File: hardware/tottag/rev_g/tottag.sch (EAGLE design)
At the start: 156 parts, among them J1 MICRO_USB_B_HIROSE_ZX62-B-5PA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, J2 CON_MICRO_SDDM3AT-SF-PEJM5, J3 TC2030-JLINK-NL, J4 TC2030-JLINK-NL, J5 TC2030-JLINK-NL, J7 TC2030-JLINK-NL, T1 HHM1595A1, U1 DW1000, U10 STM32F091CC, U11 AB1815-T3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

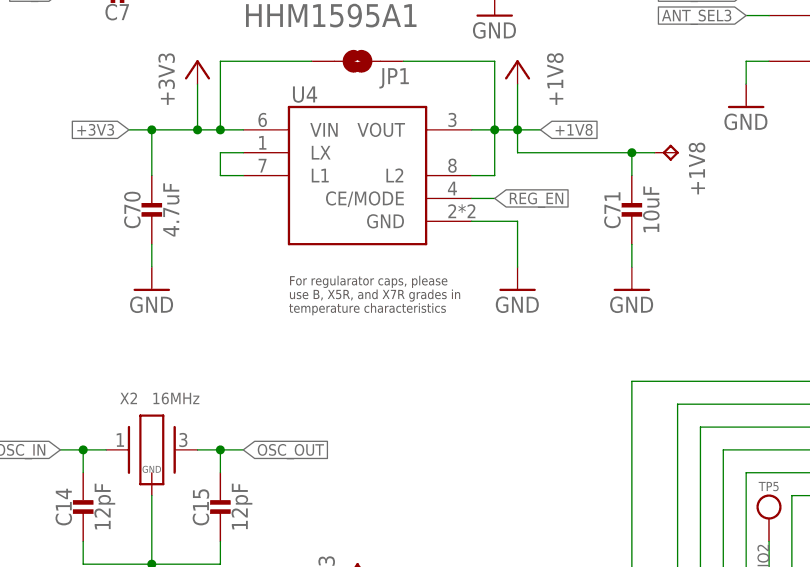
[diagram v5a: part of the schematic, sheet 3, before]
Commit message: rev_g: [WIP] Update planes; move BLE antenna
This location should keep the antenna from being covered by the primary battery
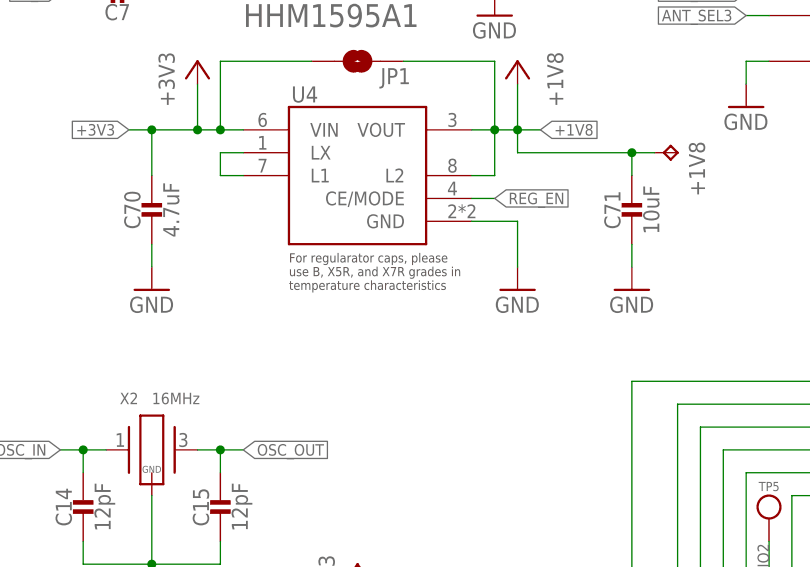
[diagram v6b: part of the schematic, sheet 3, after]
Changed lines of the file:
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@@
 for (DEEP)SLEEP</text>
 <text x="12.7" y="58.42" size="2.032" layer="98" rot="R180">VDD/48</text>
-<text x="38.1" y="137.16" size="1.016" layer="97">For regularator caps, please
+<text x="38.1" y="139.7" size="1.016" layer="97">For regularator caps, please
 use B, X5R, and X7R grades in
 temperature characteristics</text>

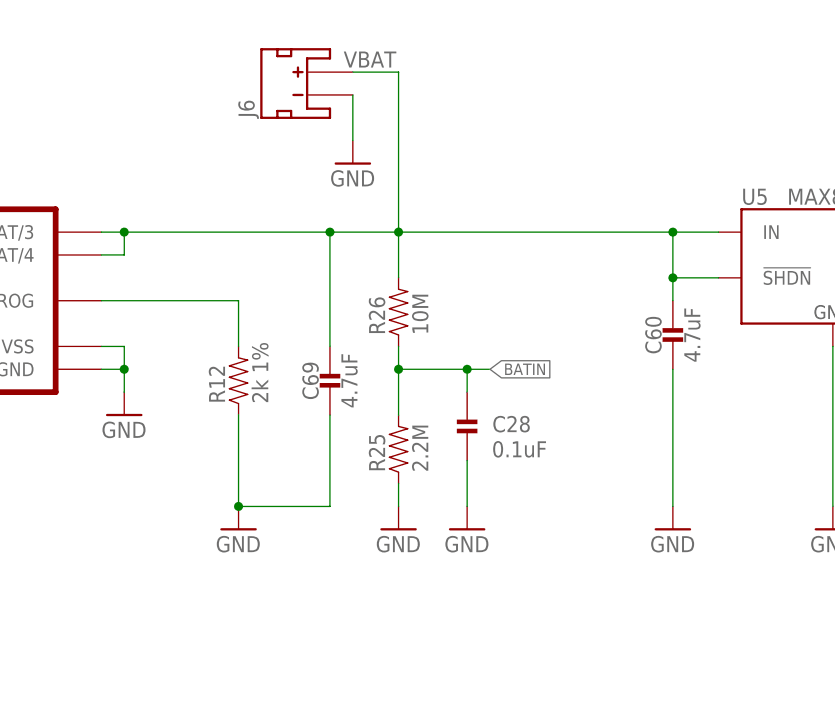
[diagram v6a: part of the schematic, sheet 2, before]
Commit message: rev_g: [WIP] add main power switch
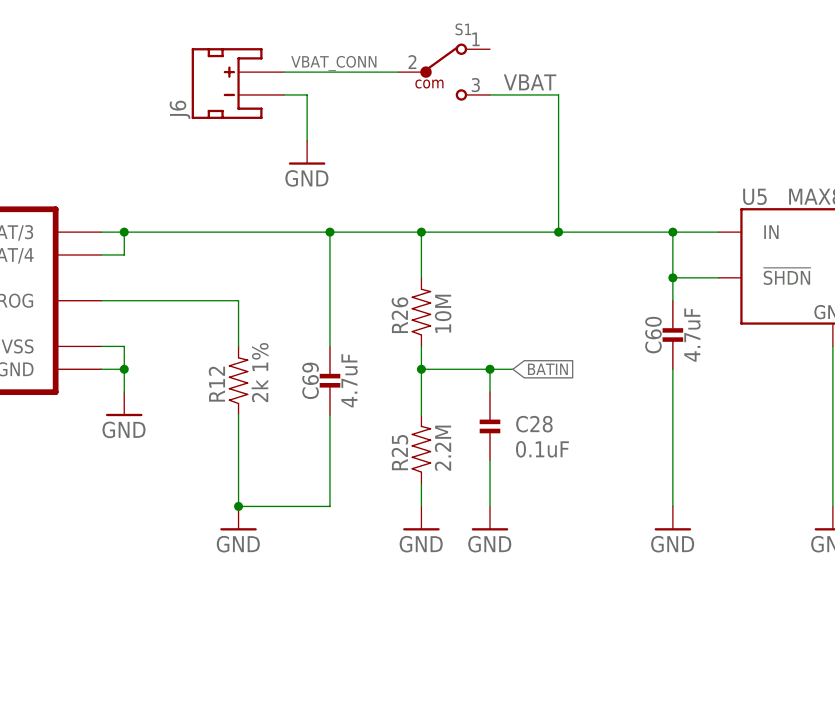
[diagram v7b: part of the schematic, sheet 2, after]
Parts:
- added S1: (no value), Wurth_Switch_WS-SLSU:450404015514
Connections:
- new net VBAT_CONN: J6.+, S1.2
- net VBAT: now also S1.3; no longer J6.+
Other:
- note added: "New case battery: PKCELL LP103450"
- note added: "To nRF ADC"
- moved on the sheet: C28, J6, R25, R26
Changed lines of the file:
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@@
 <part name="+3V5" library="regulators" deviceset="+3V3" device=""/>
 <part name="SUPPLY30" library="regulators" deviceset="GND" device=""/>
+<part name="S1" library="Wurth_Switch_WS-SLSU" library_urn="urn:adsk.eagle:library:18253886" deviceset="450404015514" device="" package3d_urn="urn:adsk.eagle:package:18253889/2"/>
 </parts>
 <sheets>
@@
 for optimal performance</text>
 <text x="222.758" y="140.97" size="1.778" layer="98" rot="R180" align="bottom-center">90 Ohm</text>
-<text x="112.522" y="179.07" size="1.778" layer="98" align="center-right">"Standard" battery is
+<text x="104.902" y="184.15" size="1.778" layer="98" align="center-right">"Standard" battery is
 PKCELL LP803860
 1528-1857-ND</text>
+<text x="104.902" y="173.99" size="1.778" layer="98" align="center-right">New case battery:
+PKCELL LP103450
+</text>
+<text x="146.304" y="149.098" size="1.27" layer="98">To nRF ADC</text>
 </plain>
 <instances>
@@
 <attribute name="VALUE" x="203.2" y="165.1" size="1.778" layer="96" rot="R90"/>
 </instance>
-<instance part="R26" gate="G$1" x="132.08" y="154.94" smashed="yes" rot="R90">
-<attribute name="NAME" x="130.5814" y="151.13" size="1.778" layer="95" rot="R90"/>
-<attribute name="VALUE" x="135.382" y="151.13" size="1.778" layer="96" rot="R90"/>
-</instance>
-<instance part="R25" gate="G$1" x="132.08" y="139.7" smashed="yes" rot="R90">
-<attribute name="NAME" x="130.5814" y="135.89" size="1.778" layer="95" rot="R90"/>
-<attribute name="VALUE" x="135.382" y="135.89" size="1.778" layer="96" rot="R90"/>
+<instance part="R26" gate="G$1" x="134.62" y="154.94" smashed="yes" rot="R90">
+<attribute name="NAME" x="133.1214" y="151.13" size="1.778" layer="95" rot="R90"/>
+<attribute name="VALUE" x="137.922" y="151.13" size="1.778" layer="96" rot="R90"/>
+</instance>
+<instance part="R25" gate="G$1" x="134.62" y="139.7" smashed="yes" rot="R90">
+<attribute name="NAME" x="133.1214" y="135.89" size="1.778" layer="95" rot="R90"/>
+<attribute name="VALUE" x="137.922" y="135.89" size="1.778" layer="96" rot="R90"/>
 </instance>
 <instance part="C60" gate="G$1" x="162.56" y="152.4" smashed="yes">
@@
 <attribute name="VALUE" x="207.01" y="151.13" size="1.778" layer="96" ratio="12" rot="R270" align="bottom-center"/>
 </instance>
-<instance part="C28" gate="G$1" x="139.7" y="139.7" smashed="yes" rot="R180">
-<attribute name="NAME" x="146.812" y="142.113" size="1.778" layer="95" rot="R180"/>
-<attribute name="VALUE" x="148.59" y="139.319" size="1.778" layer="96" rot="R180"/>
+<instance part="C28" gate="G$1" x="142.24" y="139.7" smashed="yes" rot="R180">
+<attribute name="NAME" x="149.352" y="142.113" size="1.778" layer="95" rot="R180"/>
+<attribute name="VALUE" x="151.13" y="139.319" size="1.778" layer="96" rot="R180"/>
 </instance>
 <instance part="SUPPLY3" gate="1" x="27.94" y="129.54" smashed="yes">
 <attribute name="VALUE" x="25.4" y="127" size="1.778" layer="96"/>
 </instance>
-<instance part="SUPPLY4" gate="1" x="132.08" y="129.54" smashed="yes">
-<attribute name="VALUE" x="129.54" y="127" size="1.778" layer="96"/>
-</instance>
-<instance part="SUPPLY7" gate="1" x="139.7" y="129.54" smashed="yes">
-<attribute name="VALUE" x="137.16" y="127" size="1.778" layer="96"/>
+<instance part="SUPPLY4" gate="1" x="134.62" y="129.54" smashed="yes">
+<attribute name="VALUE" x="132.08" y="127" size="1.778" layer="96"/>
+</instance>
+<instance part="SUPPLY7" gate="1" x="142.24" y="129.54" smashed="yes">
+<attribute name="VALUE" x="139.7" y="127" size="1.778" layer="96"/>
 </instance>
 <instance part="D1" gate="G$1" x="48.26" y="152.4" smashed="yes">
@@
 <attribute name="VALUE" x="12.7" y="144.78" size="1.778" layer="95" rot="MR0"/>
 </instance>
-<instance part="SUPPLY8" gate="1" x="127" y="170.18" smashed="yes">
-<attribute name="VALUE" x="124.46" y="167.64" size="1.778" layer="96"/>
+<instance part="SUPPLY8" gate="1" x="121.92" y="170.18" smashed="yes">
+<attribute name="VALUE" x="119.38" y="167.64" size="1.778" layer="96"/>
 </instance>
 <instance part="U5" gate="G$1" x="180.34" y="160.02" smashed="yes">
@@
 <attribute name="VALUE" x="230.378" y="158.75" size="1.778" layer="96" rot="R270"/>
 </instance>
-<instance part="J6" gate="G$1" x="121.92" y="177.8" smashed="yes" rot="R90">
-<attribute name="NAME" x="116.078" y="175.26" size="1.778" layer="95" rot="R90"/>
+<instance part="J6" gate="G$1" x="114.3" y="177.8" smashed="yes" rot="R90">
+<attribute name="NAME" x="108.458" y="175.26" size="1.778" layer="95" rot="R90"/>
+</instance>
+<instance part="S1" gate="G$1" x="137.16" y="180.34" smashed="yes">
+<attribute name="VALUE" x="134.75" y="175.22" size="1.27" layer="96"/>
+<attribute name="NAME" x="139.3" y="184.45" size="1.27" layer="95" align="bottom-center"/>
 </instance>
 </instances>
@@
 <pinref part="R25" gate="G$1" pin="1"/>
 <pinref part="SUPPLY4" gate="1" pin="GND"/>
-<wire x1="132.08" y1="134.62" x2="132.08" y2="132.08" width="0.1524" layer="91"/>
+<wire x1="134.62" y1="134.62" x2="134.62" y2="132.08" width="0.1524" layer="91"/>
 </segment>
 <segment>
 <pinref part="C28" gate="G$1" pin="1"/>
 <pinref part="SUPPLY7" gate="1" pin="GND"/>
-<wire x1="139.7" y1="137.16" x2="139.7" y2="132.08" width="0.1524" layer="91"/>
+<wire x1="142.24" y1="137.16" x2="142.24" y2="132.08" width="0.1524" layer="91"/>
 </segment>
 <segment>
@@
 <segment>
 <pinref part="SUPPLY8" gate="1" pin="GND"/>
-<wire x1="127" y1="172.72" x2="127" y2="177.8" width="0.1524" layer="91"/>
+<wire x1="121.92" y1="172.72" x2="121.92" y2="177.8" width="0.1524" layer="91"/>
+<wire x1="121.92" y1="177.8" x2="119.38" y2="177.8" width="0.1524" layer="91"/>
 <pinref part="J6" gate="G$1" pin="-"/>
 </segment>
@@
 <pinref part="R26" gate="G$1" pin="2"/>
 <wire x1="101.6" y1="162.56" x2="124.46" y2="162.56" width="0.1524" layer="91"/>
-<wire x1="124.46" y1="162.56" x2="132.08" y2="162.56" width="0.1524" layer="91"/>
-<wire x1="132.08" y1="162.56" x2="132.08" y2="157.48" width="0.1524" layer="91"/>
+<wire x1="124.46" y1="162.56" x2="134.62" y2="162.56" width="0.1524" layer="91"/>
+<wire x1="134.62" y1="162.56" x2="134.62" y2="157.48" width="0.1524" layer="91"/>
 <pinref part="C60" gate="G$1" pin="1"/>
 <wire x1="162.56" y1="154.94" x2="162.56" y2="157.48" width="0.1524" layer="91"/>
 <wire x1="162.56" y1="157.48" x2="162.56" y2="162.56" width="0.1524" layer="91"/>
-<wire x1="132.08" y1="162.56" x2="162.56" y2="162.56" width="0.1524" layer="91"/>
-<junction x="132.08" y="162.56"/>
+<wire x1="134.62" y1="162.56" x2="149.86" y2="162.56" width="0.1524" layer="91"/>
+<junction x="134.62" y="162.56"/>
 <junction x="162.56" y="162.56"/>
-<wire x1="132.08" y1="180.34" x2="132.08" y2="162.56" width="0.1524" layer="91"/>
-<wire x1="132.08" y1="180.34" x2="127" y2="180.34" width="0.1524" layer="91"/>
 <pinref part="U5" gate="G$1" pin="IN"/>
+<wire x1="149.86" y1="162.56" x2="162.56" y2="162.56" width="0.1524" layer="91"/>
 <wire x1="162.56" y1="162.56" x2="167.64" y2="162.56" width="0.1524" layer="91"/>
 <pinref part="U5" gate="G$1" pin="!SHDN"/>
@@
 <wire x1="101.6" y1="160.02" x2="101.6" y2="162.56" width="0.1524" layer="91"/>
 <junction x="101.6" y="162.56"/>
-<label x="131.826" y="180.848" size="1.778" layer="95" rot="MR0"/>
+<label x="149.606" y="178.308" size="1.778" layer="95" rot="MR0"/>
 <pinref part="C69" gate="G$1" pin="1"/>
 <wire x1="124.46" y1="162.56" x2="124.46" y2="149.86" width="0.1524" layer="91"/>
 <junction x="124.46" y="162.56"/>
-<pinref part="J6" gate="G$1" pin="+"/>
+<pinref part="S1" gate="G$1" pin="3"/>
+<wire x1="142.24" y1="177.8" x2="149.86" y2="177.8" width="0.1524" layer="91"/>
+<wire x1="149.86" y1="177.8" x2="149.86" y2="162.56" width="0.1524" layer="91"/>
+<junction x="149.86" y="162.56"/>
 </segment>
 </net>
 <net name="BATIN" class="0">
 <segment>
-<label x="142.24" y="147.32" size="1.27" layer="95" xref="yes"/>
+<label x="144.78" y="147.32" size="1.27" layer="95" xref="yes"/>
 <pinref part="C28" gate="G$1" pin="2"/>
 <pinref part="R26" gate="G$1" pin="1"/>
 <pinref part="R25" gate="G$1" pin="2"/>
-<wire x1="132.08" y1="142.24" x2="132.08" y2="147.32" width="0.1524" layer="91"/>
-<wire x1="132.08" y1="147.32" x2="132.08" y2="149.86" width="0.1524" layer="91"/>
-<wire x1="132.08" y1="147.32" x2="139.7" y2="147.32" width="0.1524" layer="91"/>
-<wire x1="139.7" y1="147.32" x2="139.7" y2="144.78" width="0.1524" layer="91"/>
-<junction x="132.08" y="147.32"/>
-<wire x1="139.7" y1="147.32" x2="142.24" y2="147.32" width="0.1524" layer="91"/>
-<junction x="139.7" y="147.32"/>
+<wire x1="134.62" y1="142.24" x2="134.62" y2="147.32" width="0.1524" layer="91"/>
+<wire x1="134.62" y1="147.32" x2="134.62" y2="149.86" width="0.1524" layer="91"/>
+<wire x1="134.62" y1="147.32" x2="142.24" y2="147.32" width="0.1524" layer="91"/>
+<wire x1="142.24" y1="147.32" x2="142.24" y2="144.78" width="0.1524" layer="91"/>
+<junction x="134.62" y="147.32"/>
+<wire x1="142.24" y1="147.32" x2="144.78" y2="147.32" width="0.1524" layer="91"/>
+<junction x="142.24" y="147.32"/>
 </segment>
 </net>
@@
 </segment>
 </net>
+<net name="VBAT_CONN" class="0">
+<segment>
+<pinref part="J6" gate="G$1" pin="+"/>
+<pinref part="S1" gate="G$1" pin="2"/>
+<wire x1="119.38" y1="180.34" x2="132.08" y2="180.34" width="0.1524" layer="91"/>
+<label x="120.142" y="180.848" size="1.27" layer="95"/>
+</segment>
+</net>

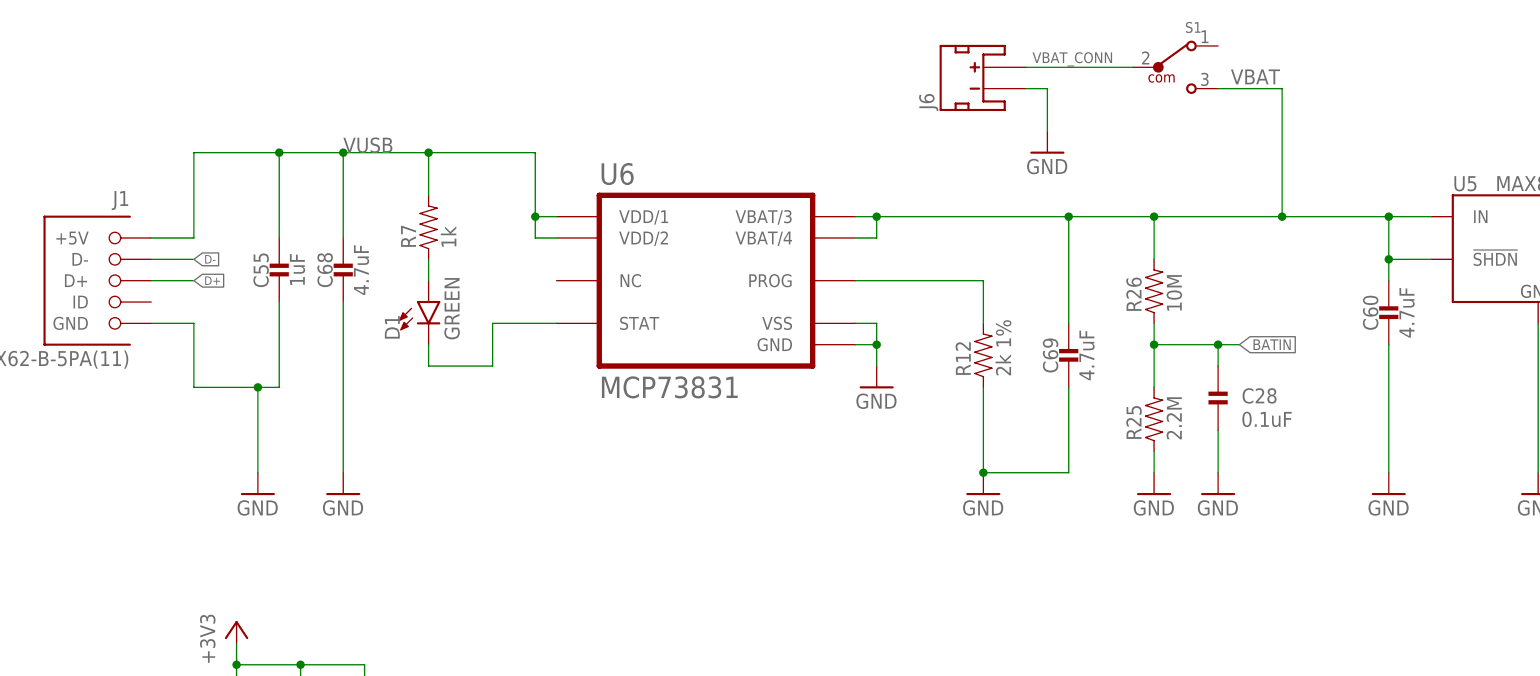
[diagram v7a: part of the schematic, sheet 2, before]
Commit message: rev_g: [WIP] routing; fix power switch point
Don't want to be in a situation where it's possible for the battery
to not charge becuase the power switch is off. Instead of disconnecting
the battery, disconnect the `VBAT` net from the regulator. Now if the
switch is off, USB power won't work either, but that's an obvious fix
that only happens in front of your face.
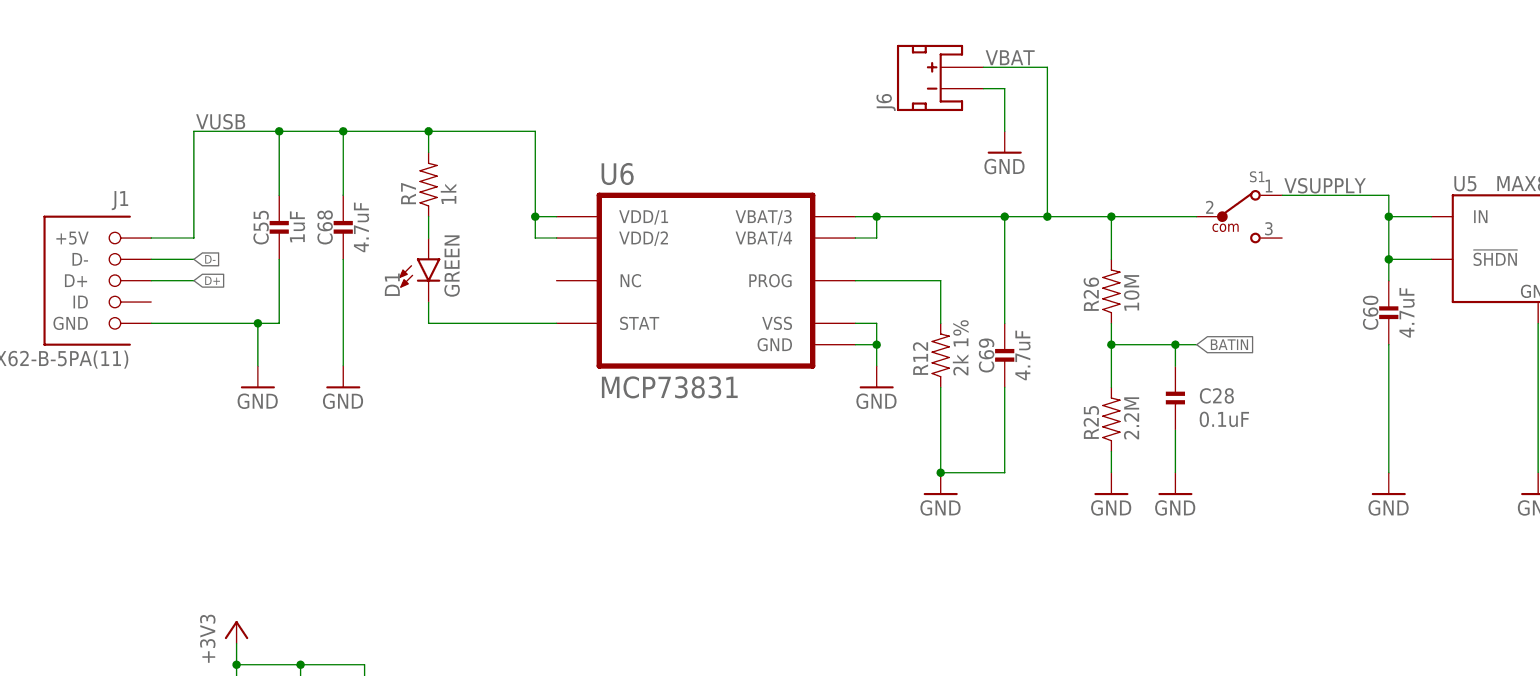
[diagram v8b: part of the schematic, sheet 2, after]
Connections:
- removed net STM_SWCLK: U10.PA14
- removed net VBAT_CONN: J6.+, S1.2
- new net VSUPPLY: C60.1, S1.1, U5.!SHDN, U5.IN
- net STM_SWDCLK: now also U10.PA14
- net VBAT: now also J6.+, S1.2; no longer C60.1, S1.3, U5.!SHDN, U5.IN
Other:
- moved on the sheet: C28, C55, C68, C69, D1, J6, R12, R25, R26, R7, S1
